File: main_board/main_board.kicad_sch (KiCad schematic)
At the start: 28 parts, among them U2 AMS1117-5.0, U4 SN32F805J/F

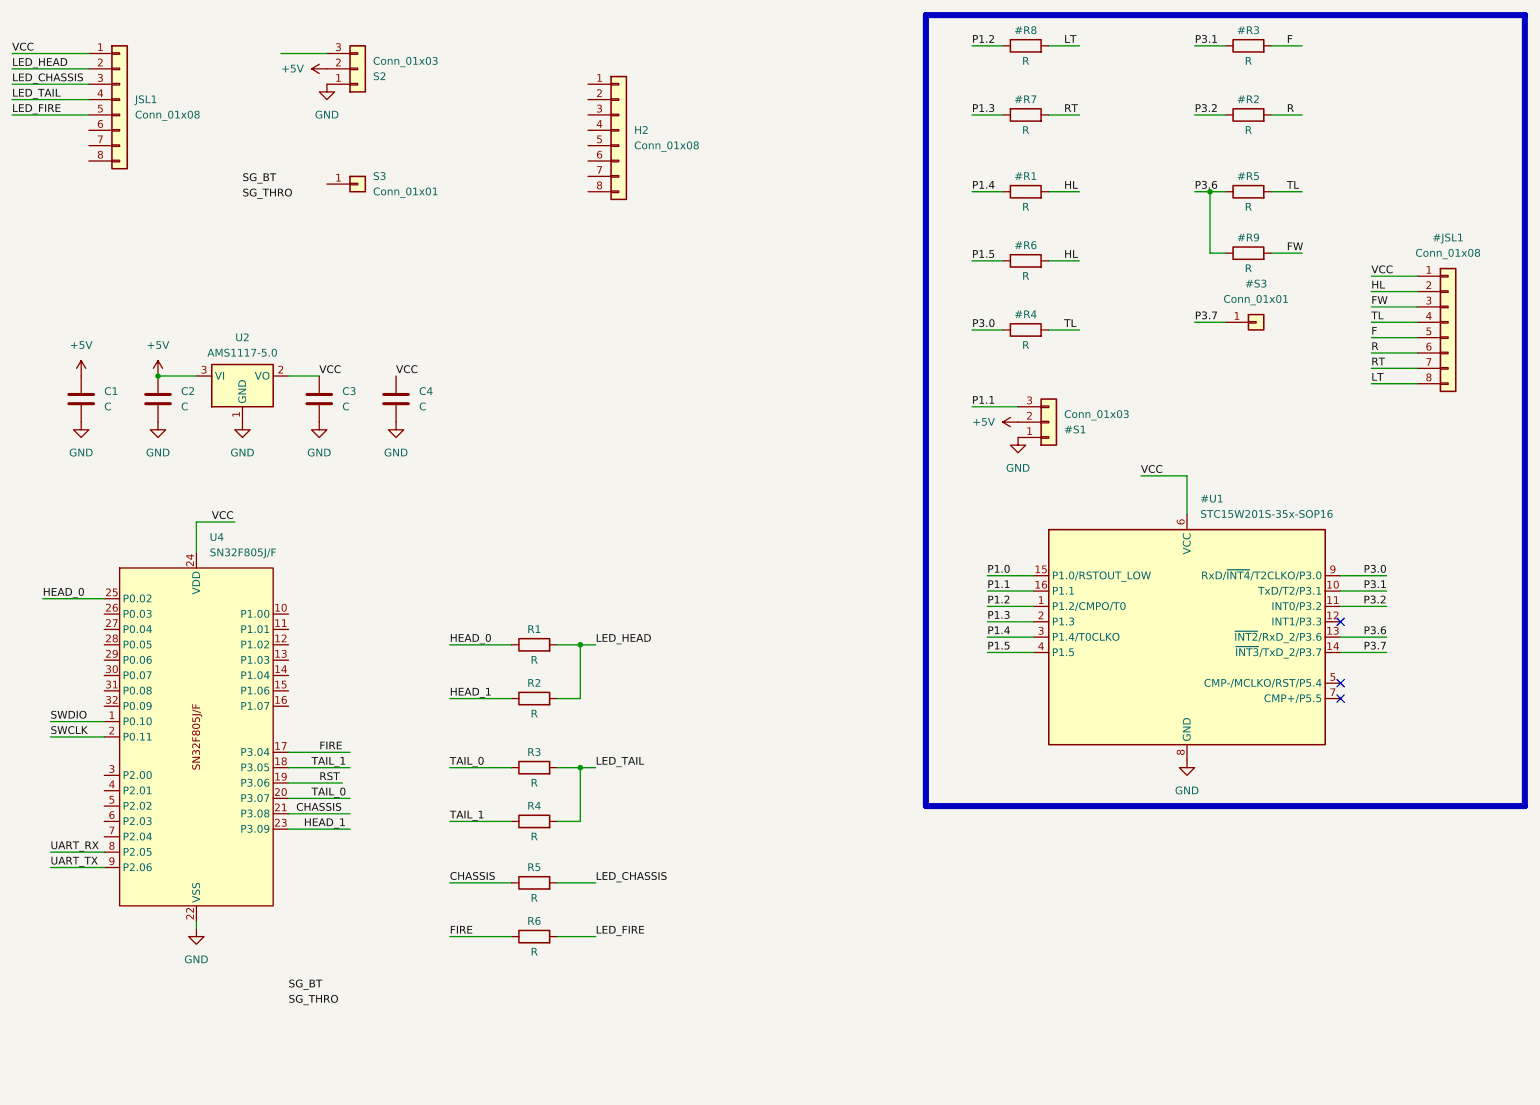
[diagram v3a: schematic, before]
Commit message: feat(board/mcu): change mcu to STM32G031G8U8
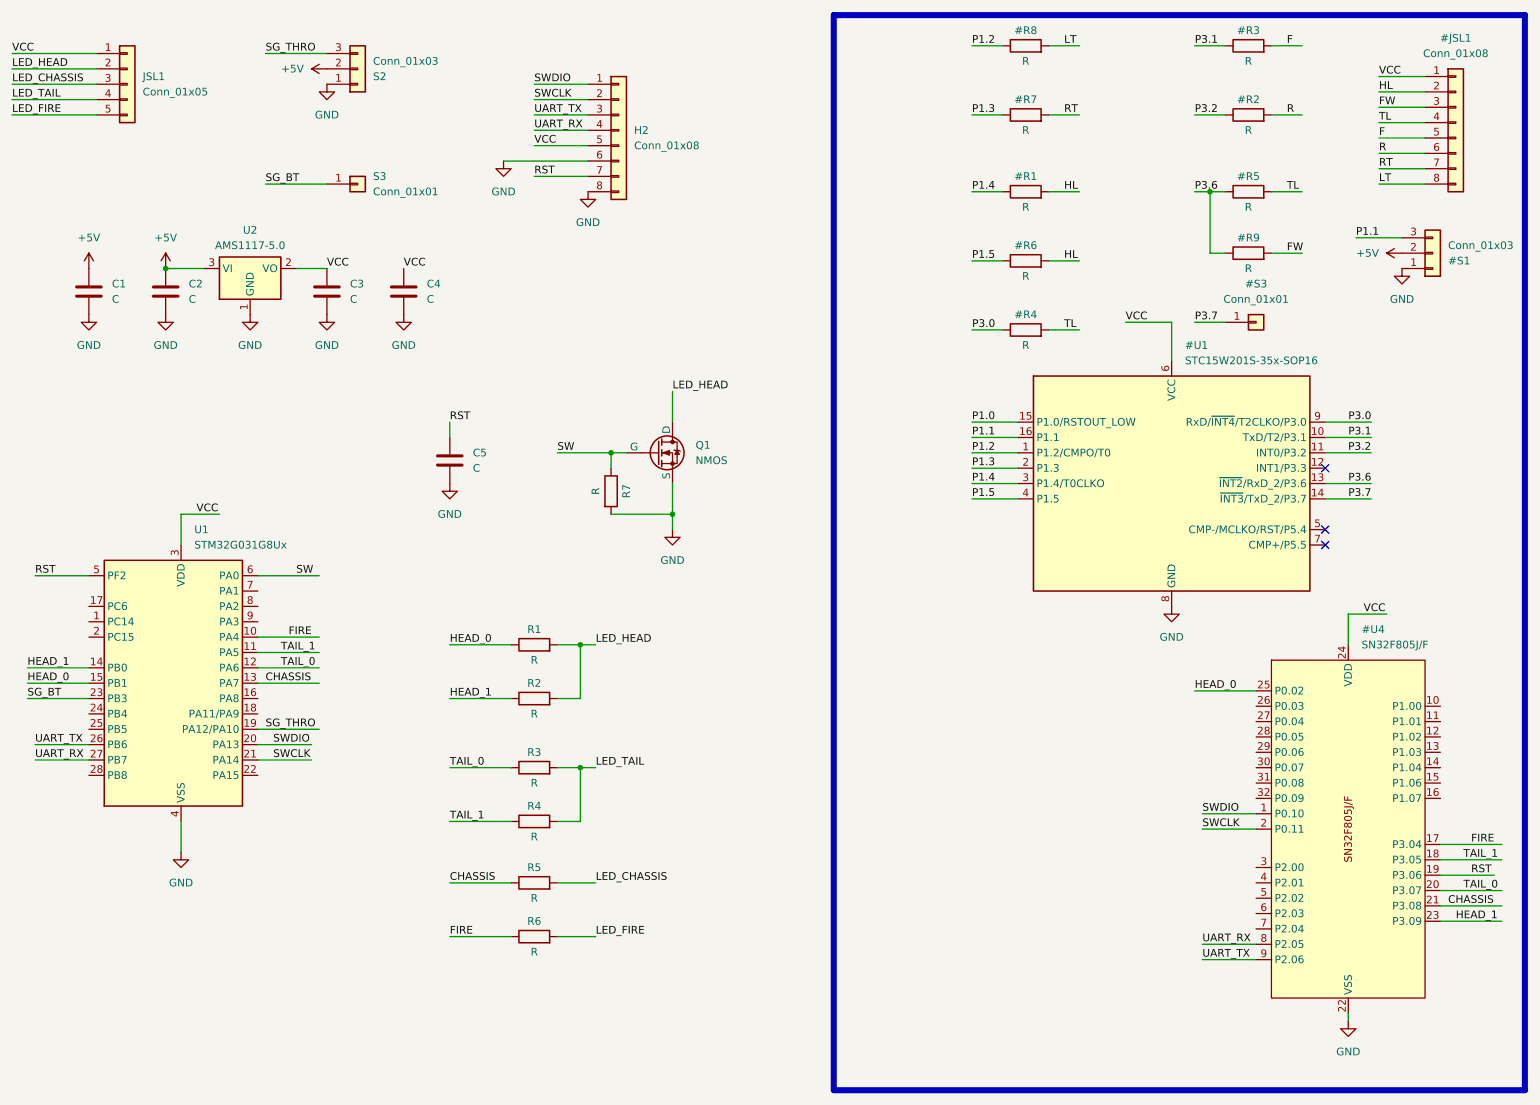
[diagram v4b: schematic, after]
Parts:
- removed JSL1: Conn_01x08, Connector_PinHeader_2.00mm:PinHeader_1x08_P2.00mm_Vertical, symbol Connector_Generic:Conn_01x08
- added C5: C, Capacitor_SMD:C_0402_1005Metric, symbol Device:C
- added JSL1: Conn_01x05, Connector_PinHeader_2.00mm:PinHeader_1x05_P2.00mm_Vertical, symbol Connector_Generic:Conn_01x05
- added Q1: NMOS, Package_TO_SOT_SMD:SOT-23, symbol Simulation_SPICE:NMOS
- added R7: R, Resistor_SMD:R_0402_1005Metric, symbol Device:R
- added U1: STM32G031G8Ux, Package_DFN_QFN:QFN-28_4x4mm_P0.5mm, symbol MCU_ST_STM32G0:STM32G031G8Ux
- renumbered U4 to #U4
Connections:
- net CHASSIS: now also U1.13 (PA7)
- net FIRE: now also U1.10 (PA4)
- net GND: now also H2.6 (Pin_6), H2.8 (Pin_8), C5.2, Q1.2 (S), R7.2, U1.4 (VSS)
- net HEAD_0: now also U1.15 (PB1)
- net HEAD_1: now also U1.14 (PB0)
- net LED_CHASSIS: now also JSL1.3 (Pin_3)
- net LED_FIRE: now also JSL1.5 (Pin_5)
- net LED_HEAD: now also JSL1.2 (Pin_2), Q1.3 (D)
- net LED_TAIL: now also JSL1.4 (Pin_4)
- net RST: now also H2.7 (Pin_7), C5.1, U1.5 (PF2)
- net SG_BT: now also S3.1 (Pin_1), U1.23 (PB3)
- net SG_THRO: now also S2.3 (Pin_3), U1.19 (PA12/PA10)
- net SWCLK: now also H2.2 (Pin_2), U1.21 (PA14)
- net SWDIO: now also H2.1 (Pin_1), U1.20 (PA13)
- net TAIL_0: now also U1.12 (PA6)
- net TAIL_1: now also U1.11 (PA5)
- net UART_RX: now also H2.4 (Pin_4), U1.27 (PB7)
- net UART_TX: now also H2.3 (Pin_3), U1.26 (PB6)
- net VCC: now also H2.5 (Pin_5), JSL1.1 (Pin_1), U1.3 (VDD)
- new net SW: Q1.1 (G), R7.1, U1.6 (PA0)
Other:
- moved on the sheet: C1, C2, C3, C4, U2

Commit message: feat(board): update ohm
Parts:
- #R1: value R -> 470
- #R2: value R -> 2k
- #R3: value R -> 150
- #R4: value R -> 82
- #R5: value R -> 820
- #R6, R1, R2, R3, R4, R5, R6, R7: value R -> 100
- #R7, #R8: value R -> 200
- #R9: value R -> 4k3
- C1, C4, C5: value C -> 100n
- C2, C3: value C -> 10u
- H2: JLCPCB (none) -> C5278509
- Q1: JLCPCB (none) -> C22463594
- U1: JLCPCB (none) -> C432211
- U2: value AMS1117-5.0 -> AMS1117-3.3; JLCPCB (none) -> C18190088
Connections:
- net GND: no longer H2.8 (Pin_8)
- net TP1: now reaches U1.1 (PC14)
- net TP1: now also H2.8 (Pin_8)

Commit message: feat(board): update JLC part number and gerber
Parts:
- C1, C4, C5: JLCPCB (none) -> C307379
- C2, C3: JLCPCB (none) -> C15850
- R1, R2, R3, R4, R5, R6, R7: JLCPCB (none) -> C77623
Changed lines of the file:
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@@
       (effects (font (size 1.27 1.27)) hide)
     )
-    (property "JLCPCB" "" (at 111.76 149.86 0)
+    (property "JLCPCB" "C77623" (at 111.76 149.86 0)
       (effects (font (size 1.27 1.27)) hide)
     )
@@
       (effects (font (size 1.27 1.27)) hide)
     )
-    (property "JLCPCB" "" (at 124.46 95.25 0)
+    (property "JLCPCB" "C77623" (at 124.46 95.25 0)
       (effects (font (size 1.27 1.27)) hide)
     )
@@
       (effects (font (size 1.27 1.27)) hide)
     )
-    (property "JLCPCB" "" (at 50.8 62.23 0)
+    (property "JLCPCB" "C15850" (at 50.8 62.23 0)
       (effects (font (size 1.27 1.27)) hide)
     )
@@
       (effects (font (size 1.27 1.27)) hide)
     )
-    (property "JLCPCB" "" (at 111.76 160.02 0)
+    (property "JLCPCB" "C77623" (at 111.76 160.02 0)
       (effects (font (size 1.27 1.27)) hide)
     )
@@
       (effects (font (size 1.27 1.27)) hide)
     )
-    (property "JLCPCB" "" (at 97.79 90.17 0)
+    (property "JLCPCB" "C307379" (at 97.79 90.17 0)
       (effects (font (size 1.27 1.27)) hide)
     )
@@
       (effects (font (size 1.27 1.27)) hide)
     )
-    (property "JLCPCB" "" (at 90.17 62.23 0)
+    (property "JLCPCB" "C307379" (at 90.17 62.23 0)
       (effects (font (size 1.27 1.27)) hide)
     )
@@
       (effects (font (size 1.27 1.27)) hide)
     )
-    (property "JLCPCB" "" (at 111.76 140.97 0)
+    (property "JLCPCB" "C77623" (at 111.76 140.97 0)
       (effects (font (size 1.27 1.27)) hide)
     )
@@
       (effects (font (size 1.27 1.27)) hide)
     )
-    (property "JLCPCB" "" (at 111.76 120.65 0)
+    (property "JLCPCB" "C77623" (at 111.76 120.65 0)
       (effects (font (size 1.27 1.27)) hide)
     )
@@
       (effects (font (size 1.27 1.27)) hide)
     )
-    (property "JLCPCB" "" (at 38.1 62.23 0)
+    (property "JLCPCB" "C307379" (at 38.1 62.23 0)
       (effects (font (size 1.27 1.27)) hide)
     )
@@
       (effects (font (size 1.27 1.27)) hide)
     )
-    (property "JLCPCB" "" (at 77.47 62.23 0)
+    (property "JLCPCB" "C15850" (at 77.47 62.23 0)
       (effects (font (size 1.27 1.27)) hide)
     )
@@
       (effects (font (size 1.27 1.27)) hide)
     )
-    (property "JLCPCB" "" (at 111.76 129.54 0)
+    (property "JLCPCB" "C77623" (at 111.76 129.54 0)
       (effects (font (size 1.27 1.27)) hide)
     )
@@
       (effects (font (size 1.27 1.27)) hide)
     )
-    (property "JLCPCB" "" (at 111.76 168.91 0)
-      (effects (font (size 1.27 1.27)) hide)
-    )
+    (property "JLCPCB" "C77623" (at 111.76 168.91 0)
+      (effects (font (size 1.27 1.27)) hide)
+    )
